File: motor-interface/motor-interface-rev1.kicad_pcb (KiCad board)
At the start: 2 copper layers, 70 x 60 mm, 43 parts, among them P1 CONN_02X12, P10 CONN_01X03, P11 CONN_01X04, P12 CONN_01X03, P13 CONN_01X03, P2 CONN_02X10, P3 CONN_01X03, P4 CONN_02X10, P5 CONN_01X04, P6 CONN_01X04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

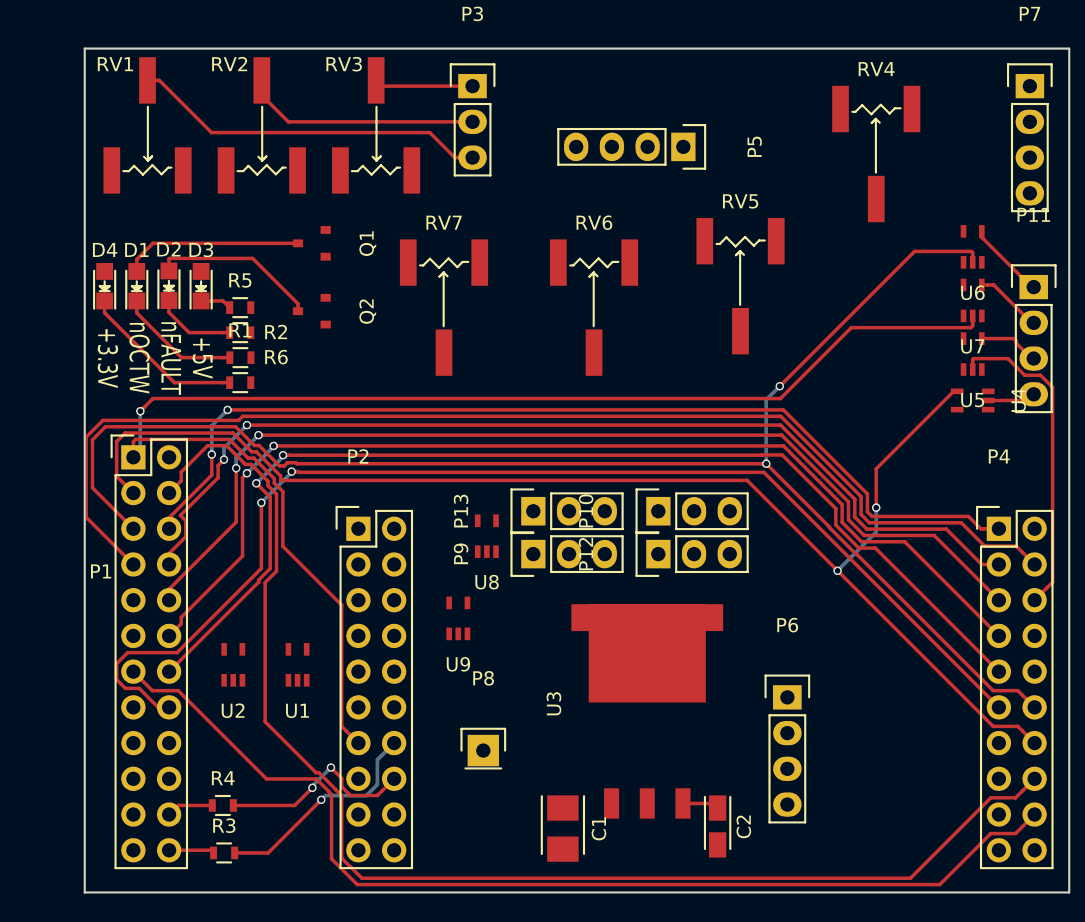
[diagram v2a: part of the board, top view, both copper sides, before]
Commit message: Finished inital track laying. still need gnd fill
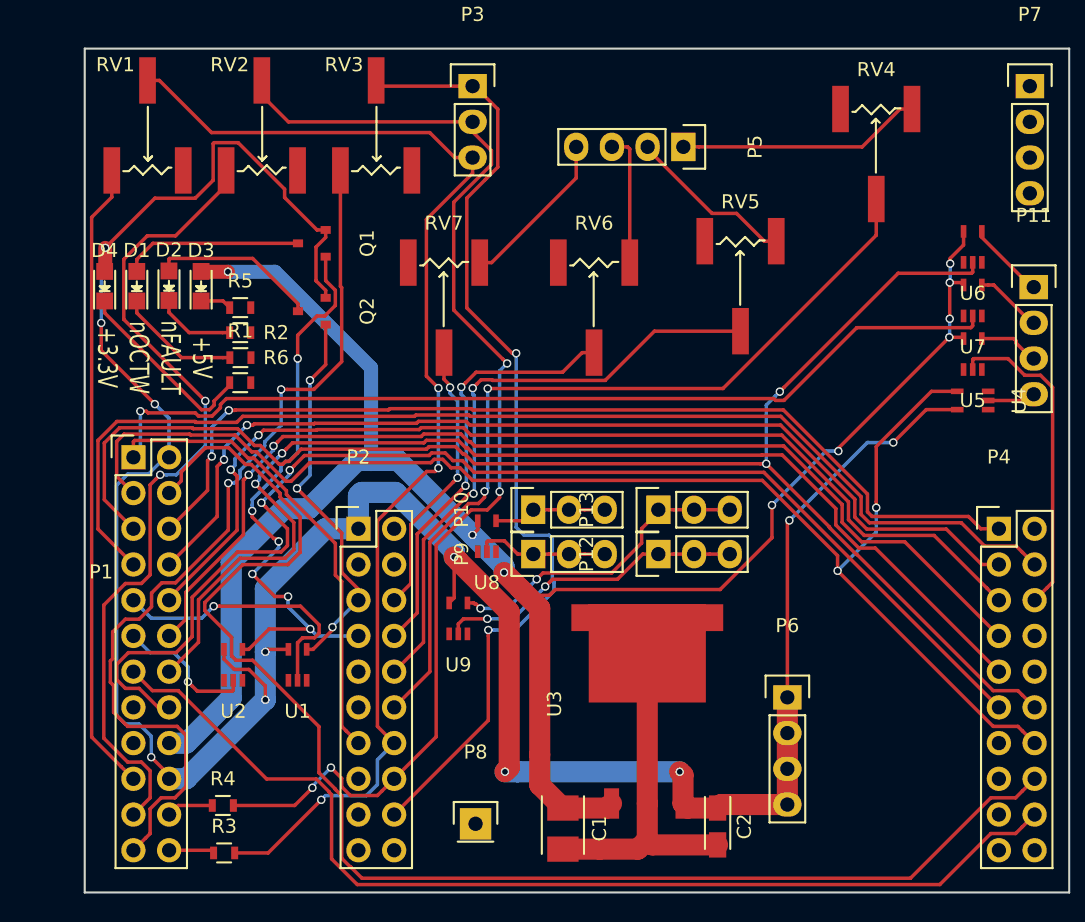
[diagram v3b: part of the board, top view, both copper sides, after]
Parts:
- moved P10 8.90 mm to (142.7, 97.2)
- moved P13 8.89 mm to (151.6, 97.2)
- moved P8 5.24 mm to (138.6, 119.5)
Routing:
- net +3V3: track 2.76 -> 197.5 mm, vias 0 -> 11
- net +5V: track 0.00 -> 136.2 mm, vias 0 -> 9
- net Net-(P1-Pad23): track 0.00 -> 64.3 mm, vias 0 -> 2
- net Net-(P2-Pad18): track 7.03 -> 70.2 mm, vias 0 -> 2
- net Net-(P2-Pad12): track 0.00 -> 60.6 mm, vias 0 -> 2
- net Net-(P1-Pad21): track 0.00 -> 59.1 mm, vias 0 -> 2
- net Net-(P2-Pad16): track 31.1 -> 85.1 mm, vias 2 -> 4
- net Net-(P2-Pad14): track 41.0 -> 87.0 mm, vias 2 -> 3
- net Net-(P1-Pad19): track 0.00 -> 45.1 mm
- net Net-(P2-Pad10): track 0.00 -> 43.5 mm, vias 0 -> 2
- net Net-(P2-Pad7): track 0.00 -> 42.6 mm, vias 0 -> 6
- net Net-(P2-Pad8): track 0.00 -> 30.4 mm, vias 0 -> 2
- net Net-(P2-Pad5): track 0.00 -> 27.5 mm, vias 0 -> 3
- net GND: track 0.00 -> 24.7 mm
- net Net-(P13-Pad1): track 0.00 -> 22.4 mm, vias 0 -> 2
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
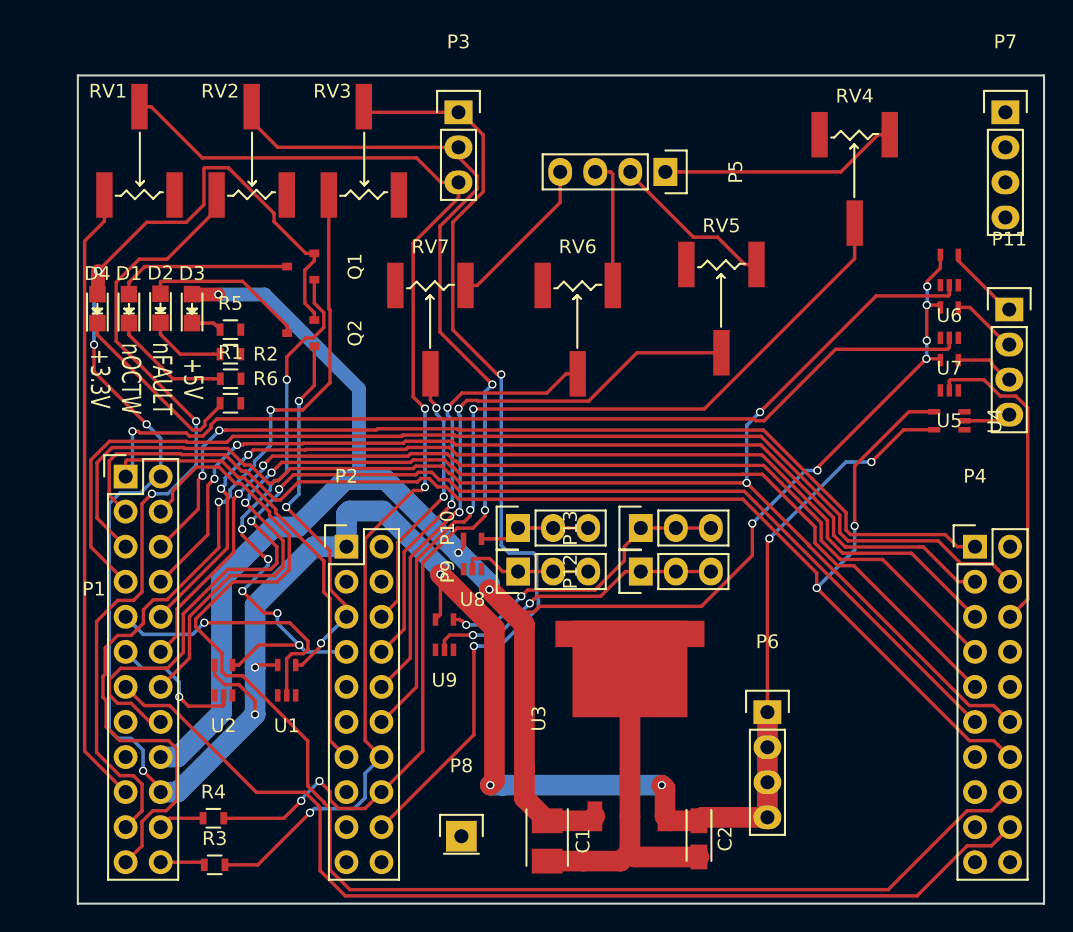
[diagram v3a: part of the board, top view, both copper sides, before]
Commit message: put in fills, moved f.fab, all connections made
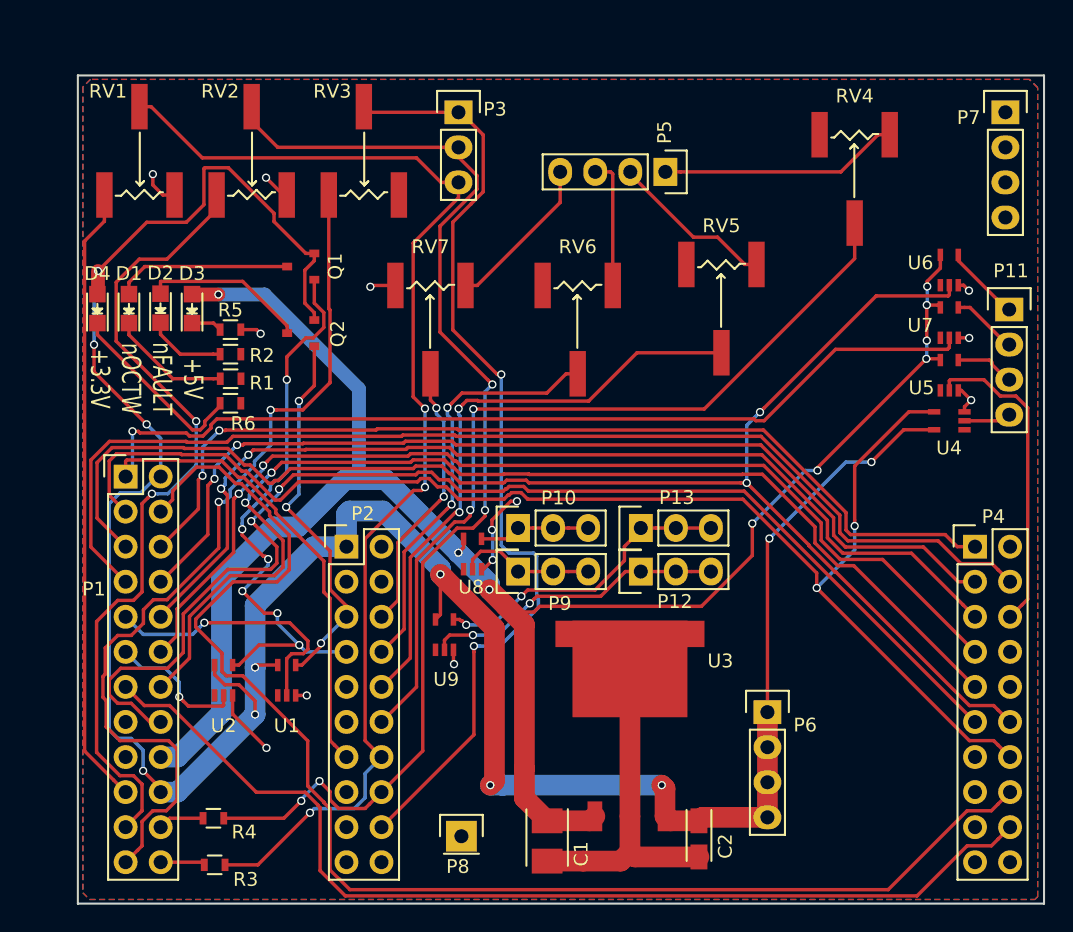
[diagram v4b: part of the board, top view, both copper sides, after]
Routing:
- net GND: track 24.7 -> 49.8 mm, vias 0 -> 13
- net Net-(P9-Pad1): track 9.50 -> 10.0 mm
- added copper zone on B.Cu, net GND
- added copper zone on F.Cu, net GND
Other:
- board text added: "Motor Control Interface Designed By: Joseph Kubeck RIT Senior Design P16261 April 2016"

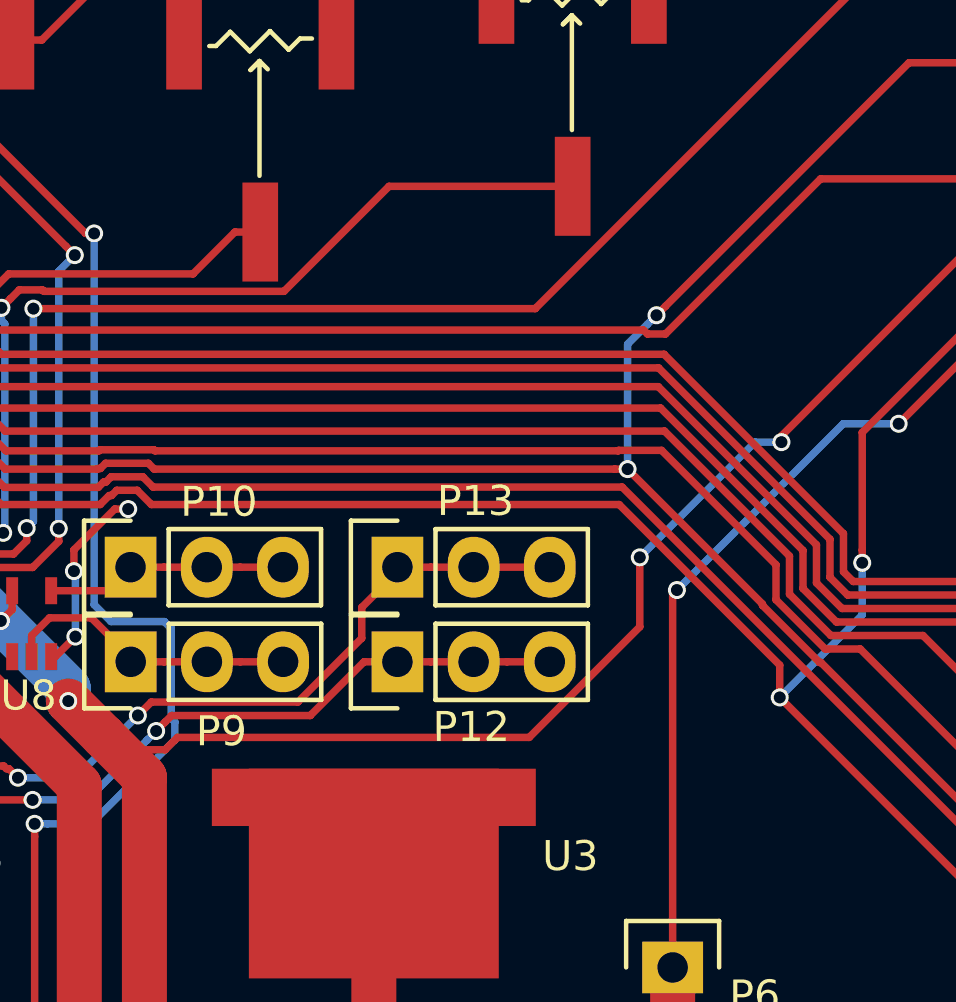
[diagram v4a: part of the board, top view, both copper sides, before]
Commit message: Added some datasheet links for completeness
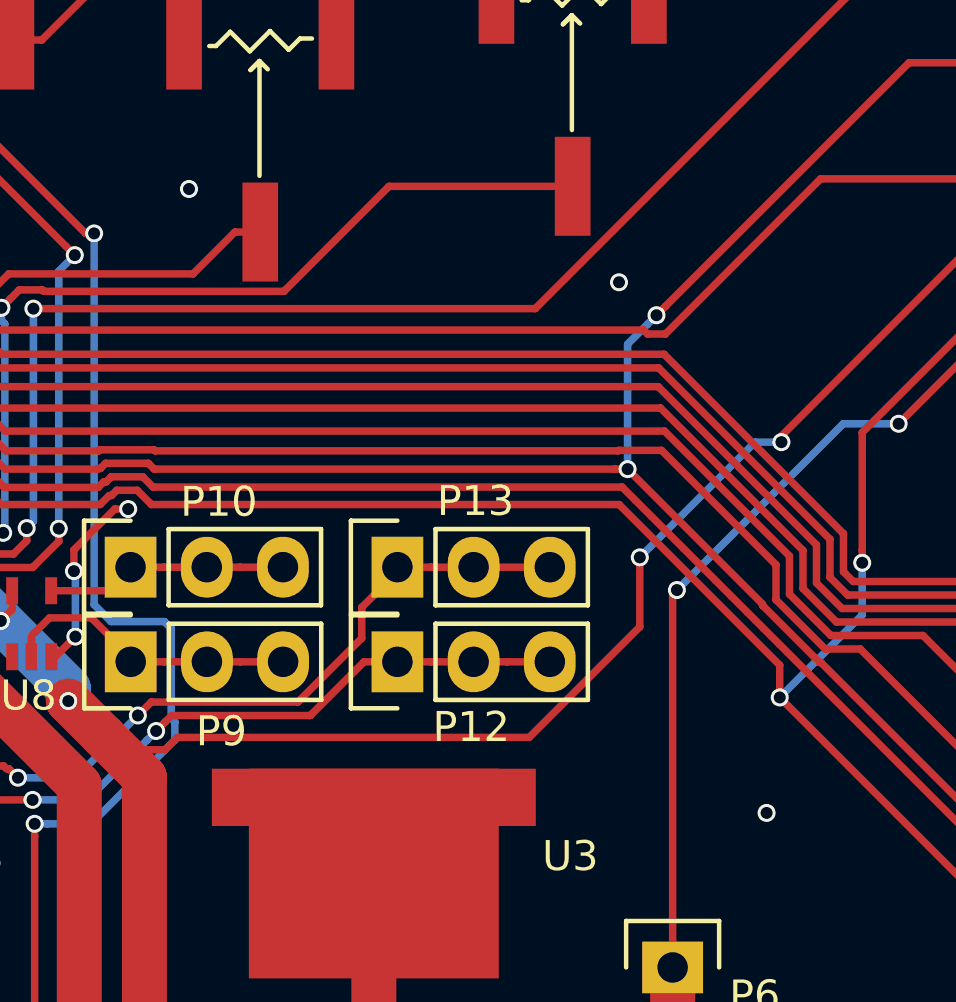
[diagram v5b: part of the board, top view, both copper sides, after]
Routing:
- net (no net): track 0.09 -> 0.21 mm, vias 0 -> 3
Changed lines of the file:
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@@
     (links 117)
     (no_connects 0)
-    (area 50.696398 60.831 183.439194 124.463001)
+    (area 110.776999 64.312999 180.927001 124.463001)
     (thickness 1.6)
     (drawings 6)
-    (tracks 948)
+    (tracks 952)
     (zones 0)
     (modules 43)
@@
       (layerselection 0x00030_80000001)
       (usegerberextensions false)
-      (excludeedgelayer true)
+      (excludeedgelayer false)
       (linewidth 0.100000)
       (plotframeref false)
-      (viasonmask false)
+      (viasonmask true)
       (mode 1)
       (useauxorigin false)
@@
       (padsonsilk false)
       (subtractmaskfromsilk false)
-      (outputformat 1)
+      (outputformat 4)
       (mirror false)
-      (drillshape 1)
+      (drillshape 0)
       (scaleselection 1)
-      (outputdirectory ""))
+      (outputdirectory "C:/Users/terminator/Documents/classwork/senior design/plots/interface board/"))
   )
   (net 0 "")
@@
   (gr_line (start 110.852 64.388) (end 180.852 64.388) (layer Edge.Cuts) (width 0.15))
   (gr_line (start 110.852 124.388) (end 110.852 64.388) (layer Edge.Cuts) (width 0.15))
+  (via (at 144.6911 84.5693) (size 0.6) (drill 0.4) (layers F.Cu B.Cu) (net 0))
+  (via (at 159.02432 87.67826) (size 0.6) (drill 0.4) (layers F.Cu B.Cu) (net 0))
+  (segment (start 163.9443 105.48112) (end 163.9443 105.36682) (width 0.25) (layer F.Cu) (net 0))
+  (via (at 163.9443 105.36682) (size 0.6) (drill 0.4) (layers F.Cu B.Cu) (net 0))
   (segment (start 51.086399 98.731399) (end 51.021399 98.796399) (width 0.25) (layer F.Cu) (net 0))
   (segment (start 174.64 87.206) (end 174.86648 87.206) (width 0.25) (layer F.Cu) (net 1))
